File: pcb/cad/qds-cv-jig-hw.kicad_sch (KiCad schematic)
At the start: 13 parts, among them J1 Conn_02x01, J10 Conn_02x01, J11 Conn_02x01, J12 Conn_01x02, J13 Conn_02x01, J2 Conn_01x02, J3 Conn_02x01, J4 Conn_02x01, J5 Conn_01x02, J6 Conn_02x01, J7 Conn_01x08, J8 Conn_02x01, J9 Conn_01x02

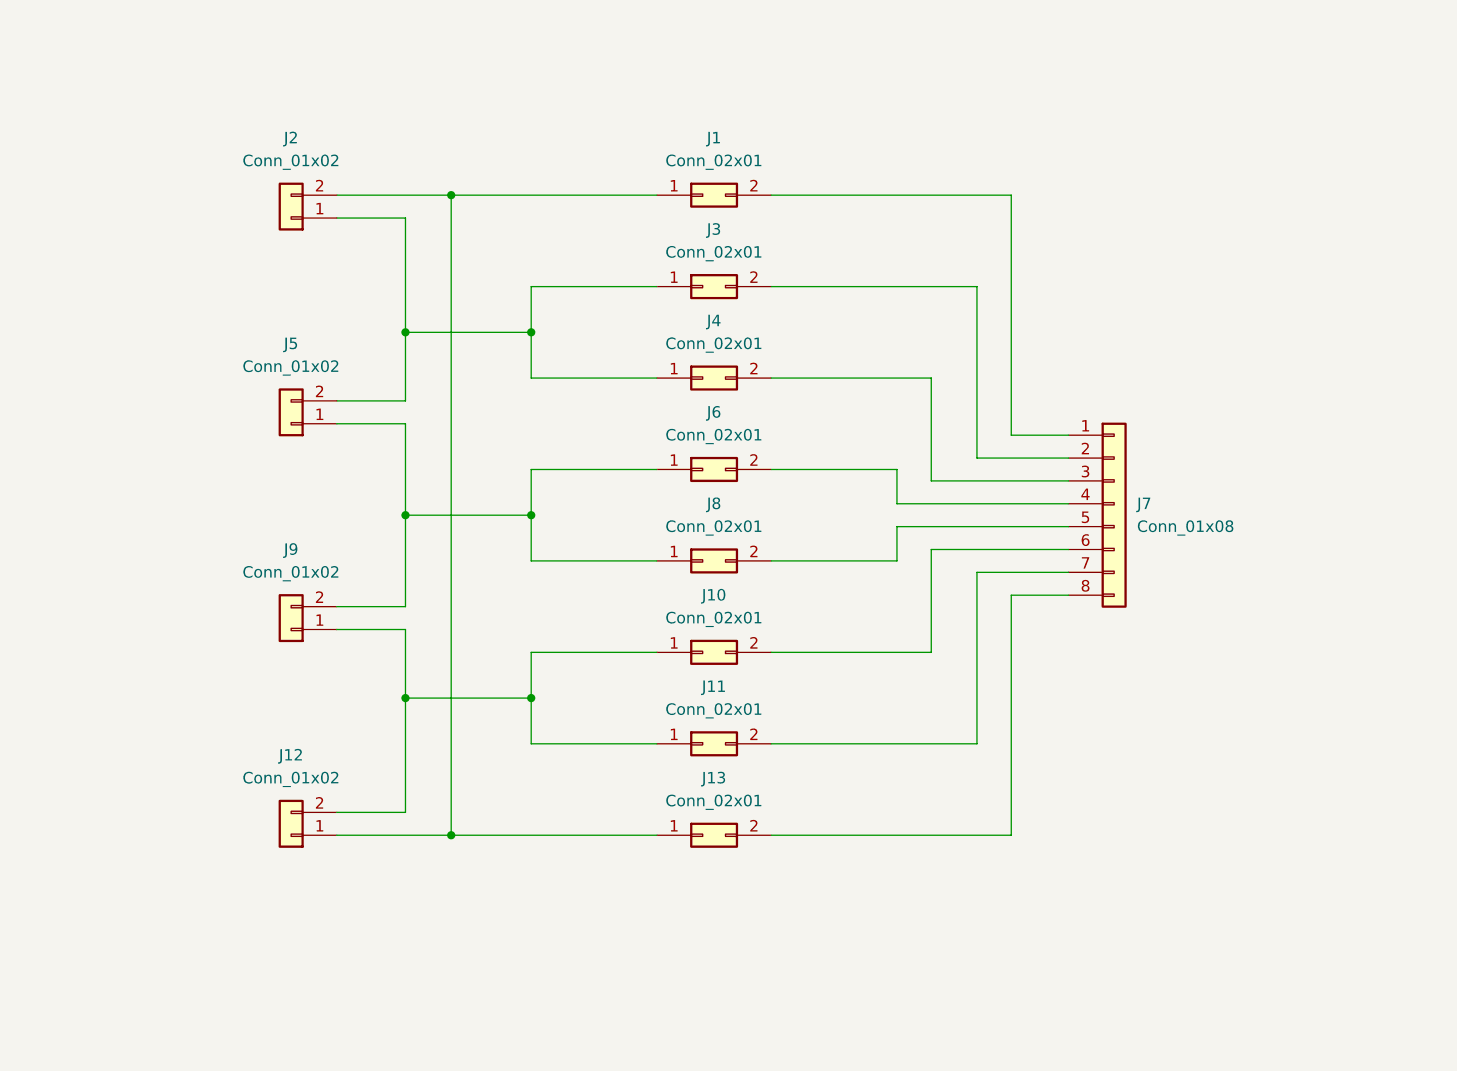
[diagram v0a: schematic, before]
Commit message: Include connectors, jumpers, tracks and mounting holes on schematics and PCB
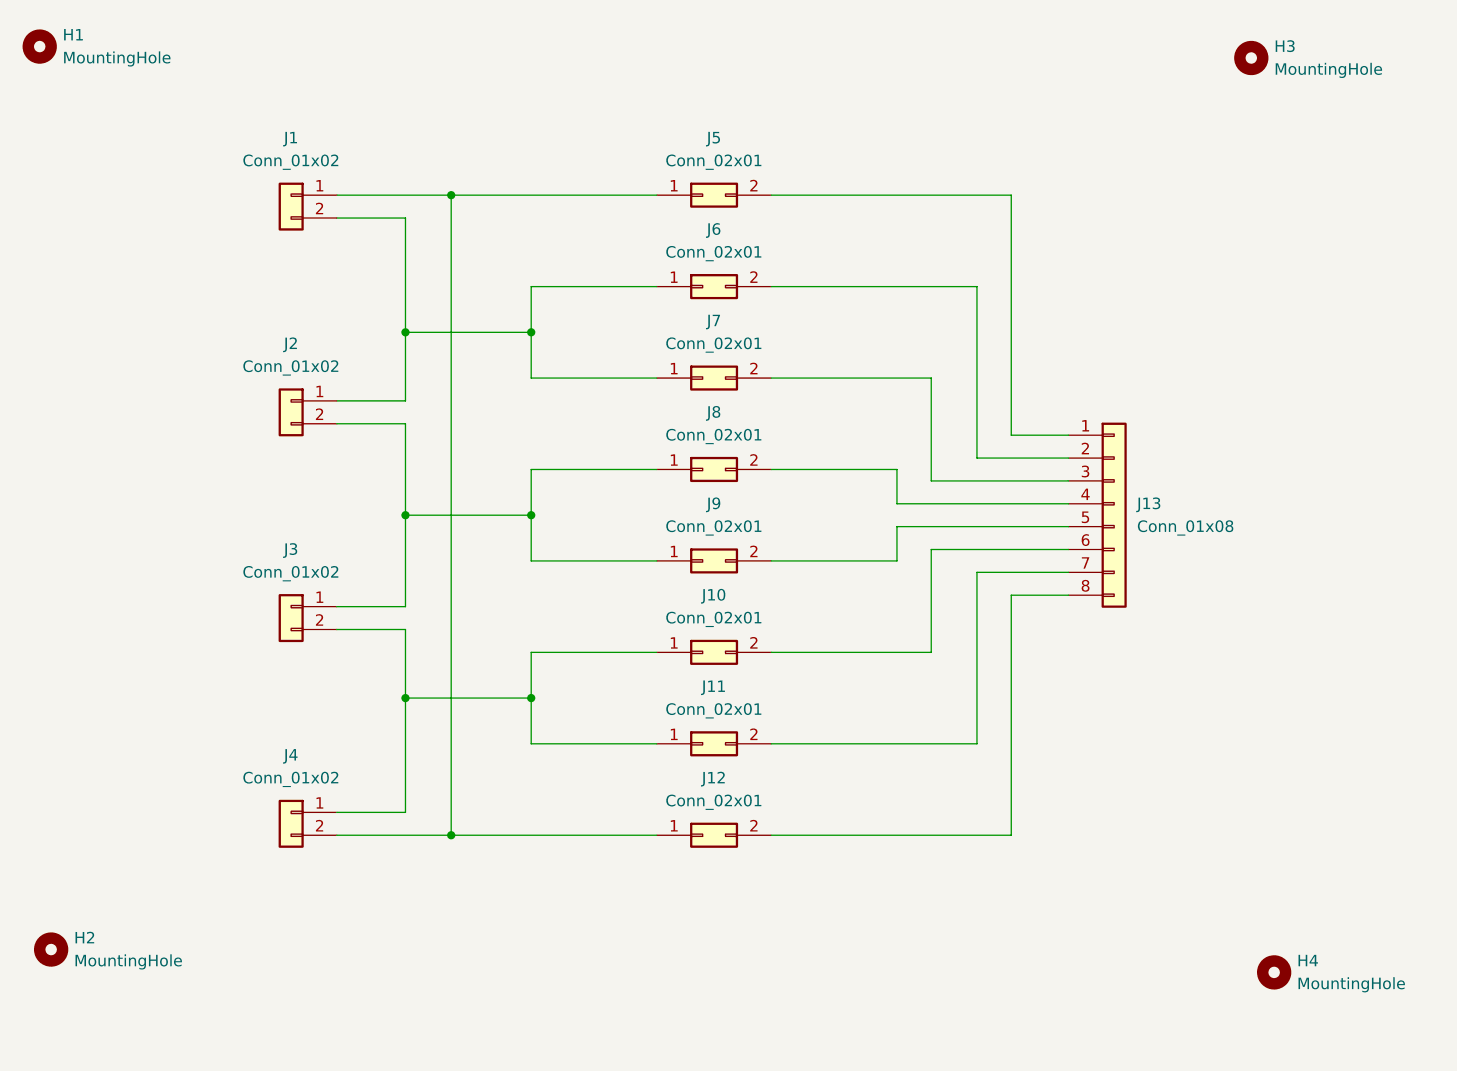
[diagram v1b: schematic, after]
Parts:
- removed J12, J5, J9: Conn_01x02, Connector_Phoenix_MSTB:PhoenixContact_MSTBVA_2,5_2-G-5,08_1x02_P5.08mm_Vertical, symbol Connector_Generic:Conn_01x02
- added H1, H2, H3, H4: MountingHole, MountingHole:MountingHole_3.2mm_M3, symbol Mechanical:MountingHole
- added J1, J3, J4: Conn_01x02, Connector_Phoenix_MSTB:PhoenixContact_MSTBVA_2,5_2-G-5,08_1x02_P5.08mm_Vertical, symbol Connector_Generic:Conn_01x02
- renumbered J13 to J12, J7 to J13, J1 to J5, J3 to J6, J4 to J7, J6 to J8, J8 to J9
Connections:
- net at J10.1 (Pin_1), J11.1 (Pin_1): now also J3.2 (Pin_2), J4.1 (Pin_1)
- net at J12.1 (Pin_1), J5.1 (Pin_1): now also J1.1 (Pin_1), J4.2 (Pin_2); no longer J2.2 (Pin_2)
- net at J8.1 (Pin_1), J9.1 (Pin_1): now also J2.2 (Pin_2), J3.1 (Pin_1)
- net at J2.1 (Pin_1), J6.1 (Pin_1), J7.1 (Pin_1): now also J1.2 (Pin_2)

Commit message: Include board outline, potentiometer and spacers, place GND fill
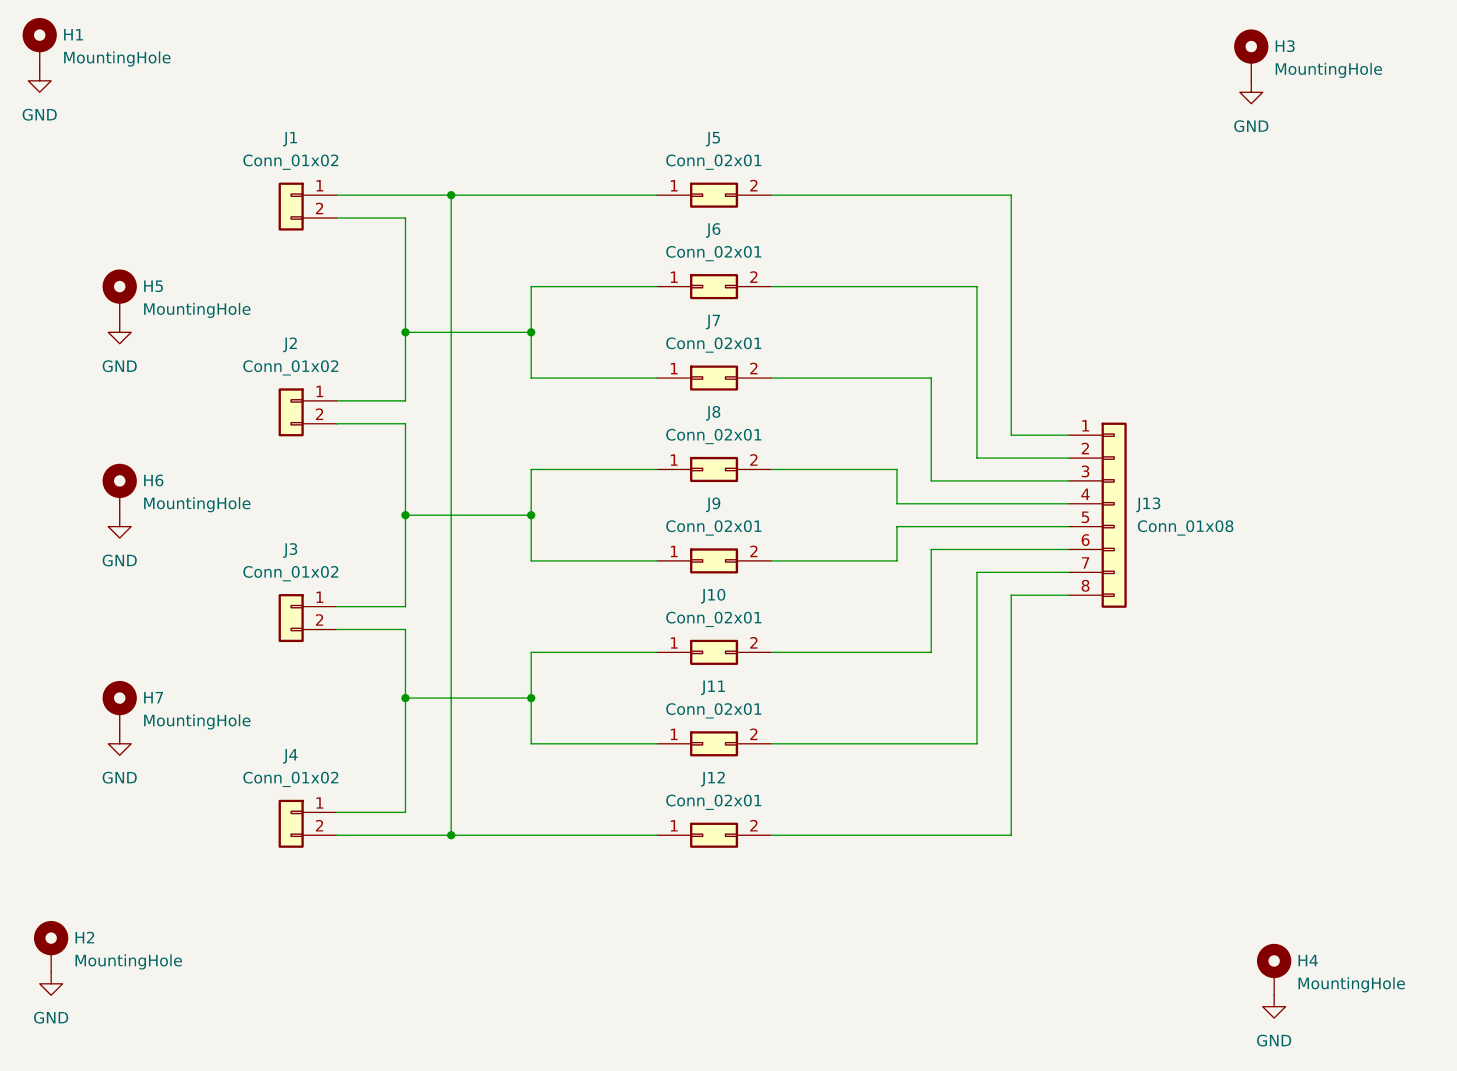
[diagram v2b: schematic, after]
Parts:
- added H5, H6, H7: MountingHole, qds-cv-jig-hw-lib:Potentiometer_Vishay_534, symbol Mechanical:MountingHole_Pad
- H1, H2, H3, H4: footprint MountingHole:MountingHole_3.2mm_M3 -> MountingHole:MountingHole_3.2mm_M3_Pad; symbol Mechanical:MountingHole -> Mechanical:MountingHole_Pad
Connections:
- new net GND: H1.1, H2.1, H3.1, H4.1, H5.1, H6.1, H7.1
